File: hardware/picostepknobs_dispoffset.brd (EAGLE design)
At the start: 177.8 x 81.3 mm, 57 parts, among them J1 AUDIO-JACK-TRRS, J2 AUDIO-JACK-TRRS, P1 10k, P2 10k, P3 10k, P4 10k, P5 10k, P6 10k, P7 10k, P8 10k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

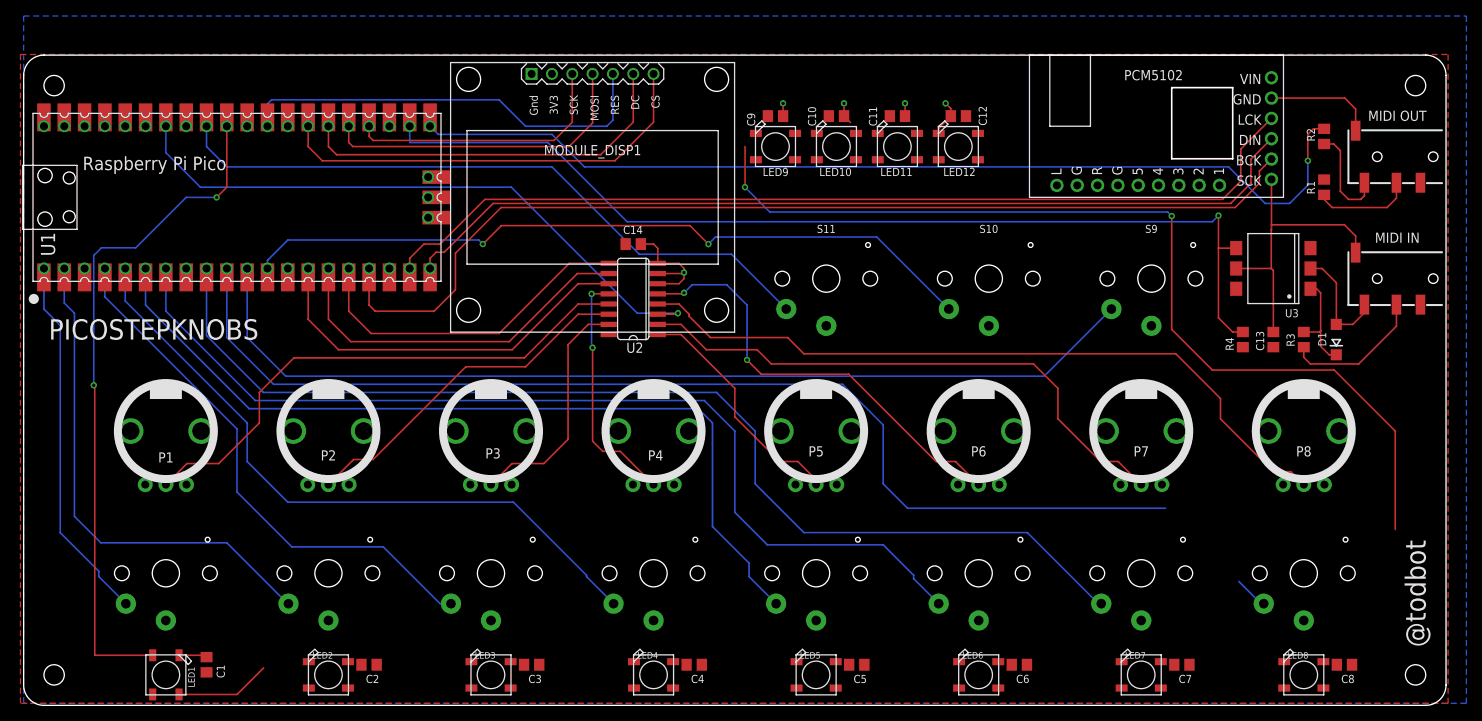
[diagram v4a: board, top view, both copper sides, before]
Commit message: keep proto version for posterity
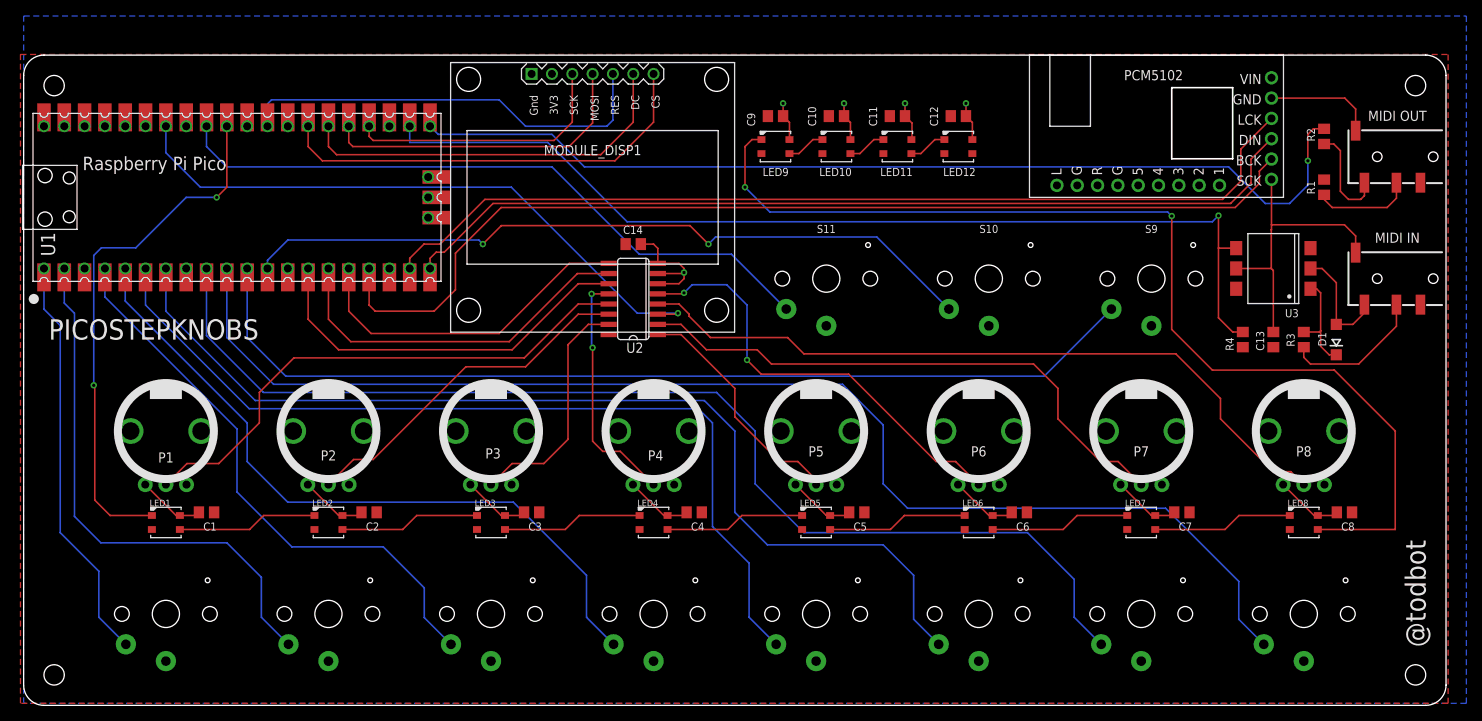
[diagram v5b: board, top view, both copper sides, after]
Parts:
- LED1, LED10, LED11, LED12, LED2, LED3, LED4, LED5, LED6, LED7, LED8, LED9: value WS2812B5050 -> WS2812B3535; device todstuff2023:WS2812B -> todstuff2023:LED3535
- moved LED1 19.1 mm to (17.8, 22.9), turned to 0 degrees
- moved LED2 19.1 mm to (38.1, 22.9)
- moved LED3 19.1 mm to (58.4, 22.9)
- moved LED4 19.1 mm to (78.7, 22.9)
- moved LED5 19.1 mm to (99.1, 22.9)
- moved LED6 19.1 mm to (119.4, 22.9)
- moved LED7 19.1 mm to (139.7, 22.9)
- moved LED8 19.1 mm to (160.0, 22.9)
- moved C1 19.0 mm to (22.9, 24.1), turned to 180 degrees
- moved C2 19.0 mm to (43.2, 24.1)
- moved C3 19.0 mm to (63.5, 24.1)
- moved C4 19.0 mm to (83.8, 24.1)
- moved C5 19.0 mm to (104.1, 24.1)
- moved C6 19.0 mm to (124.5, 24.1)
- moved C7 19.0 mm to (144.8, 24.1)
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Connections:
- net +3V3: now also LED1.2, LED10.2, LED11.2, LED12.2, LED2.2, LED3.2, LED4.2, LED5.2, LED6.2, LED7.2, LED8.2, LED9.2; no longer LED1.1-VDD, LED10.1-VDD, LED11.1-VDD, LED12.1-VDD, LED2.1-VDD, LED3.1-VDD, LED4.1-VDD, LED5.1-VDD, LED6.1-VDD, LED7.1-VDD, LED8.1-VDD, LED9.1-VDD
- net GND: now also LED1.4, LED10.4, LED11.4, LED12.4, LED2.4, LED3.4, LED4.4, LED5.4, LED6.4, LED7.4, LED8.4, LED9.4; no longer LED1.3-GND, LED10.3-GND, LED11.3-GND, LED12.3-GND, LED2.3-GND, LED3.3-GND, LED4.3-GND, LED5.3-GND, LED6.3-GND, LED7.3-GND, LED8.3-GND, LED9.3-GND
- net N$1: now also LED1.3, LED2.1; no longer LED1.2-DOUT, LED2.4-DIN
- net N$10: now also LED4.3, LED5.1; no longer LED4.2-DOUT, LED5.4-DIN
- net N$11: now also LED5.3, LED6.1; no longer LED5.2-DOUT, LED6.4-DIN
- net N$12: now also LED6.3, LED7.1; no longer LED6.2-DOUT, LED7.4-DIN
- net N$13: now also LED7.3, LED8.1; no longer LED7.2-DOUT, LED8.4-DIN
- net N$14: now also LED10.1, LED9.3; no longer LED10.4-DIN, LED9.2-DOUT
- net N$15: now also LED10.3, LED11.1; no longer LED10.2-DOUT, LED11.4-DIN
- net N$16: now also LED11.3, LED12.1; no longer LED11.2-DOUT, LED12.4-DIN
- net N$17: now also LED8.3, LED9.1; no longer LED8.2-DOUT, LED9.4-DIN
- net N$2: now also LED2.3, LED3.1; no longer LED2.2-DOUT, LED3.4-DIN
- net N$4: now also LED3.3, LED4.1; no longer LED3.2-DOUT, LED4.4-DIN
- net NEOPIXEL: now also LED1.1; no longer LED1.4-DIN
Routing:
- net GND: track 93.2 -> 162.6 mm
- net NEOPIXEL: track 86.2 -> 67.5 mm
- net SW8: track 144.5 -> 162.3 mm
- net N$13: track 0.00 -> 17.5 mm
- net N$10: track 0.00 -> 17.5 mm
- net N$2: track 0.00 -> 17.5 mm
- net N$4: track 0.00 -> 17.5 mm
- net N$12: track 0.00 -> 17.5 mm
- net N$11: track 0.00 -> 17.5 mm
- net N$17: track 119.6 -> 131.7 mm
- net N$1: track 11.9 -> 17.5 mm
- net SW1: track 47.3 -> 52.3 mm
- net SW6: track 124.4 -> 129.5 mm
- net SW5: track 108.5 -> 113.6 mm
- net SW4: track 84.8 -> 89.9 mm
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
